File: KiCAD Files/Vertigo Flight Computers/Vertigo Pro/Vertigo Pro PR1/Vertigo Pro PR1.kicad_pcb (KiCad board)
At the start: 4 copper layers, 45.2 x 81.8 mm, 150 parts, among them IC1 ICM-20602, IC2 DPS310XTSA1, J1 ST-LINK Conn, J2 USB_C_2.0, J3 FFC2A32-24-T, J4 Screw_Terminal, J5 Screw_Terminal, J6 Screw_Terminal, J7 Screw_Terminal, Q1 MMBT3904-TP, Q2 MMBT3904-TP, Q3 FDN339AN, Q4 FDN339AN, Q5 SI7149ADP-T1-GE3, Q6 MMBT3904-TP, Q7 MMBT3904-TP, Q8 FDN339AN, Q9 FDN339AN, SW1 SW_SPDT, U1 STM32F103C8Tx, U10 TPS79133DBVR, U12 TLV709, U13 TLV75528PDBV, U2 AP63203WU, U3 ESP32-S3-WROOM-1, U4 TLV75515PDBV, U5 TLV709, U8 NEO-6M-GPS, U9 24AA32A-I_MS, Y1 16MHz

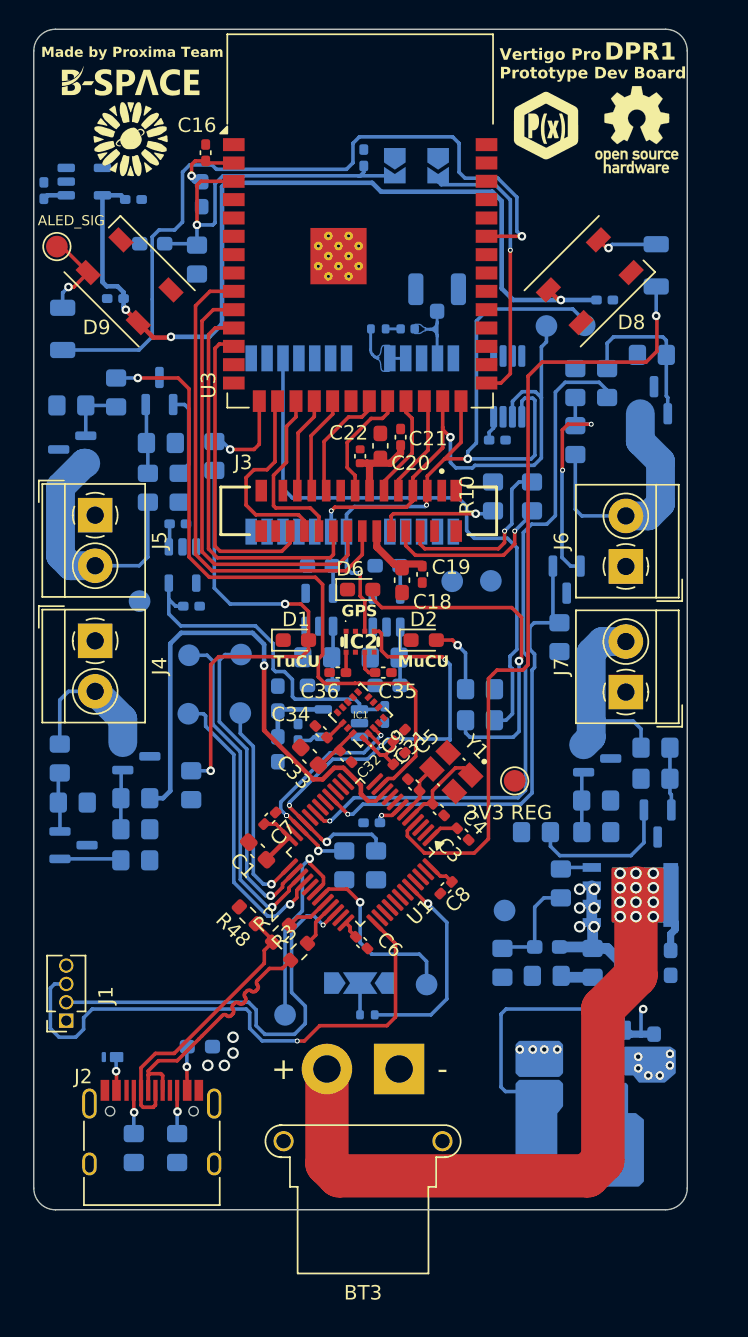
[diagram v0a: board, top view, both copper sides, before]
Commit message: Power routing
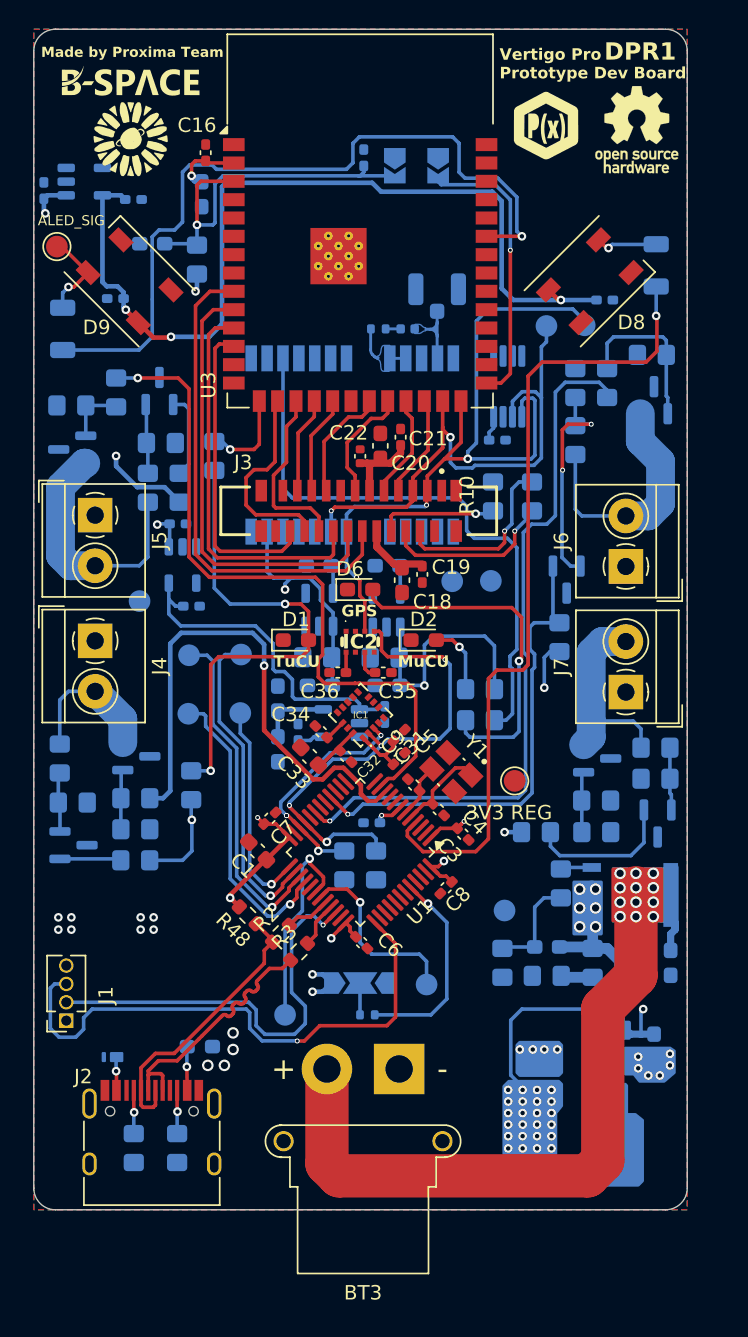
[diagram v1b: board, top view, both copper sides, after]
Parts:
- moved C24 0.07 mm to (145.7, 105.9)
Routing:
- net +3.3V: track 45.5 -> 99.4 mm, vias 1 -> 47
- net VCC: track 164.5 -> 194.5 mm, vias 11 -> 13
- net /ESP_I2C_SCL: track 72.3 -> 71.7 mm
- added copper zone on In2.Cu, net +3.3V
- added copper zone on B.Cu, net AGND
- added copper zone on F.Cu, net AGND
- added copper zone on In1.Cu, net AGND

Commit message: Much routing
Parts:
- moved ULN 7.78 mm to (141.1, 108.7)
- moved C33 0.28 mm to (144.9, 118.9)
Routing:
- net /CONTI_C2: track 5.93 -> 54.0 mm, vias 0 -> 3
- net /USB_VBUS_D_CUTOFF: track 12.1 -> 46.1 mm
- net /BATT_U: track 2.22 -> 34.2 mm, vias 0 -> 2
- net /IGN_4: track 0.00 -> 29.1 mm, vias 0 -> 3
- net /CONTI_C1: track 4.25 -> 25.7 mm, vias 0 -> 1
- net /ULN_3V3: track 9.88 -> 30.4 mm, vias 0 -> 5
- net /CONTI_C4: track 10.4 -> 28.5 mm, vias 0 -> 1
- net AGND: track 0.00 -> 5.29 mm, vias 10 -> 21
- net +3.3V: track 99.4 -> 102.3 mm, vias 47 -> 50
- net /SWCLK: track 38.8 -> 37.6 mm
- net /SWDIO: track 29.3 -> 30.4 mm
- net Net-(D1-A): track 33.9 -> 33.3 mm

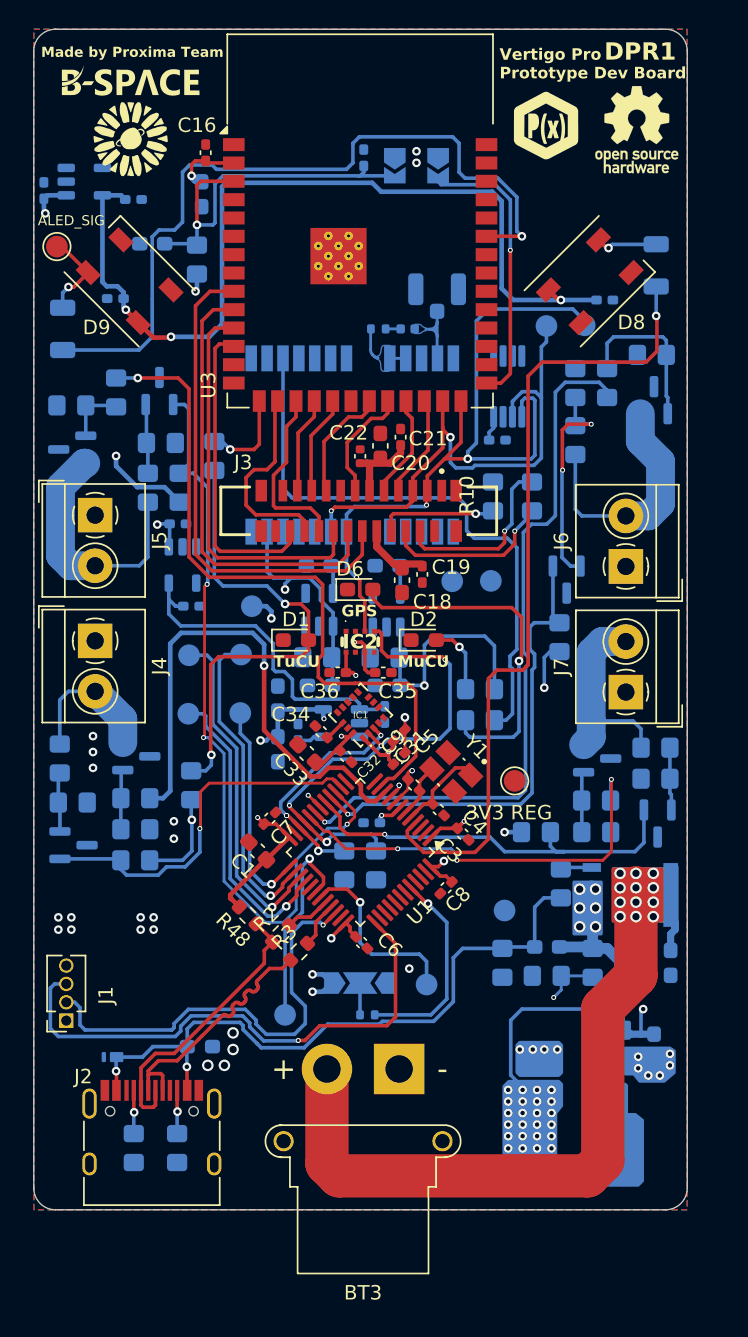
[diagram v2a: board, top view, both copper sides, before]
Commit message: Routing, EEPROM power fix + other stuff
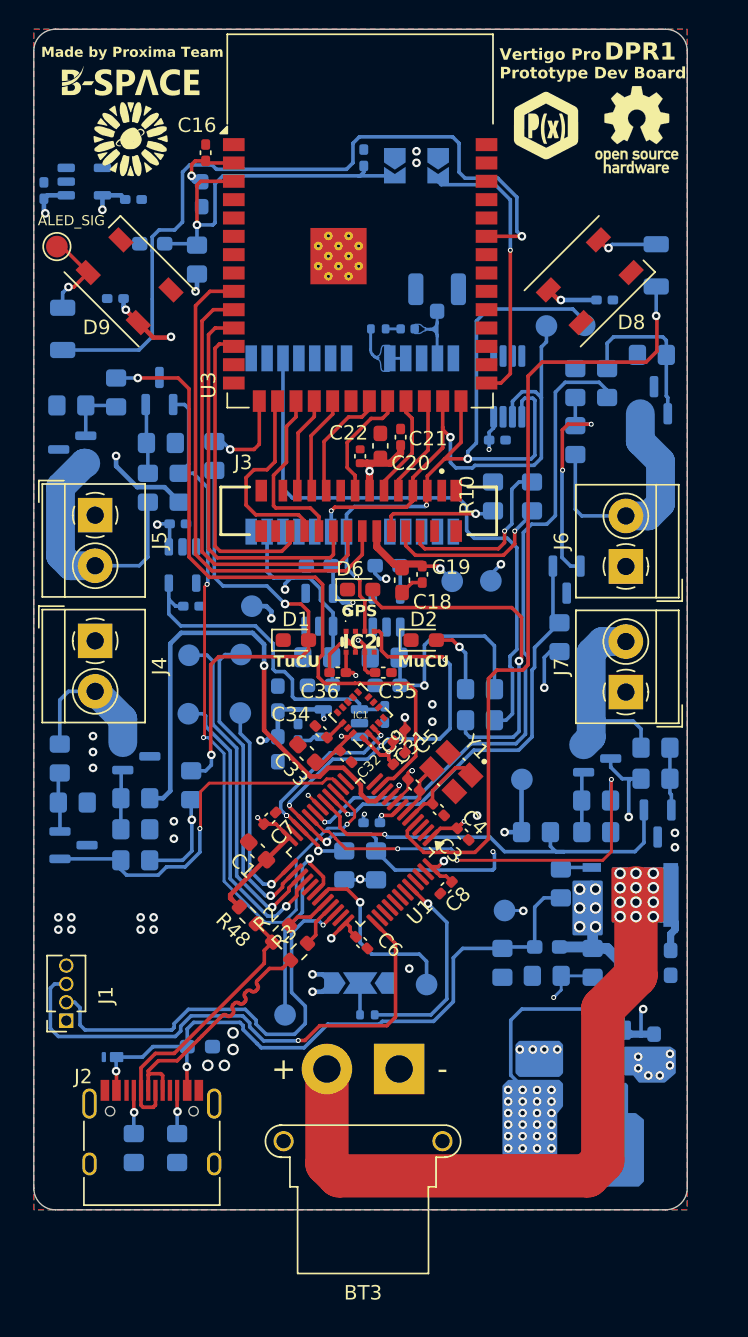
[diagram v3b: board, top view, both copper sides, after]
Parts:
- 3V3 REG: moved to B.Cu
- moved 3V3 REG 0.51 mm to (159.8, 120.7), turned to 180 degrees
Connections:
- C40 pad 2: Net-(U9-VCC) -> +3.3V
- U9 pad 8: Net-(U9-VCC) -> +3.3V
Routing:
- net /AVDD_2V8: track 20.2 -> 37.2 mm, vias 1 -> 3
- net AGND: track 5.29 -> 19.6 mm, vias 21 -> 30
- net /DVDD_1V5: track 6.74 -> 19.5 mm, vias 0 -> 2
- net /ESP_I2C_SCL: track 71.7 -> 81.8 mm, vias 6 -> 7
- net VCC: track 194.5 -> 202.9 mm, vias 13 -> 14
- net +3.3V: track 102.3 -> 110.4 mm, vias 50 -> 52
- net /ALED_PWR: track 62.1 -> 56.3 mm, vias 3 -> 4
- net /CONTI_C3: track 33.0 -> 29.4 mm
- net /IGN_3: track 49.7 -> 47.4 mm
- net Net-(U9-VCC): track 1.74 -> 0.00 mm

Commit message: Routing
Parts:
- added G***: LOGO, Vertigo Pro KiCad Libraries:proxima_logo_simple_footprint, B.Cu at (148.7, 72.2)
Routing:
- net AGND: track 19.6 -> 48.7 mm, vias 30 -> 49
- net /ESP_I2C_SDA: track 69.2 -> 82.4 mm, vias 7 -> 8
- net /ESP_I2C_SCL: track 81.8 -> 94.2 mm, vias 7 -> 8
- net /ULN_3V3: track 30.4 -> 31.4 mm
- net /AVDD_2V8: track 37.2 -> 37.9 mm
- net /CAM_RESET: track 11.9 -> 12.6 mm
- net VCC: track 202.9 -> 203.6 mm, vias 14 -> 16
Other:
- board text added: "Designed by Proxima Team"
- board text removed: "Made by Proxima Team"

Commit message: Routing
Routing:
- net /ESP_UART_TX: track 12.9 -> 77.9 mm, vias 1 -> 2
- net /ESP_UART_RX: track 14.7 -> 78.4 mm, vias 1 -> 2
- net AGND: track 48.7 -> 61.5 mm, vias 49 -> 56
- net /AVDD_2V8: track 37.9 -> 46.7 mm
- net Net-(U4-EN): track 0.00 -> 2.23 mm
- net Net-(U13-EN): track 0.00 -> 2.18 mm

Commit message: Routing
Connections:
- Q5 pad : (no net) -> Net-(BT3-+)
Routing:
- net AGND: track 61.5 -> 76.9 mm, vias 56 -> 69
- net +3.3V: track 110.4 -> 115.6 mm, vias 52 -> 54
- net /ESP_UART_TX: track 77.9 -> 78.9 mm

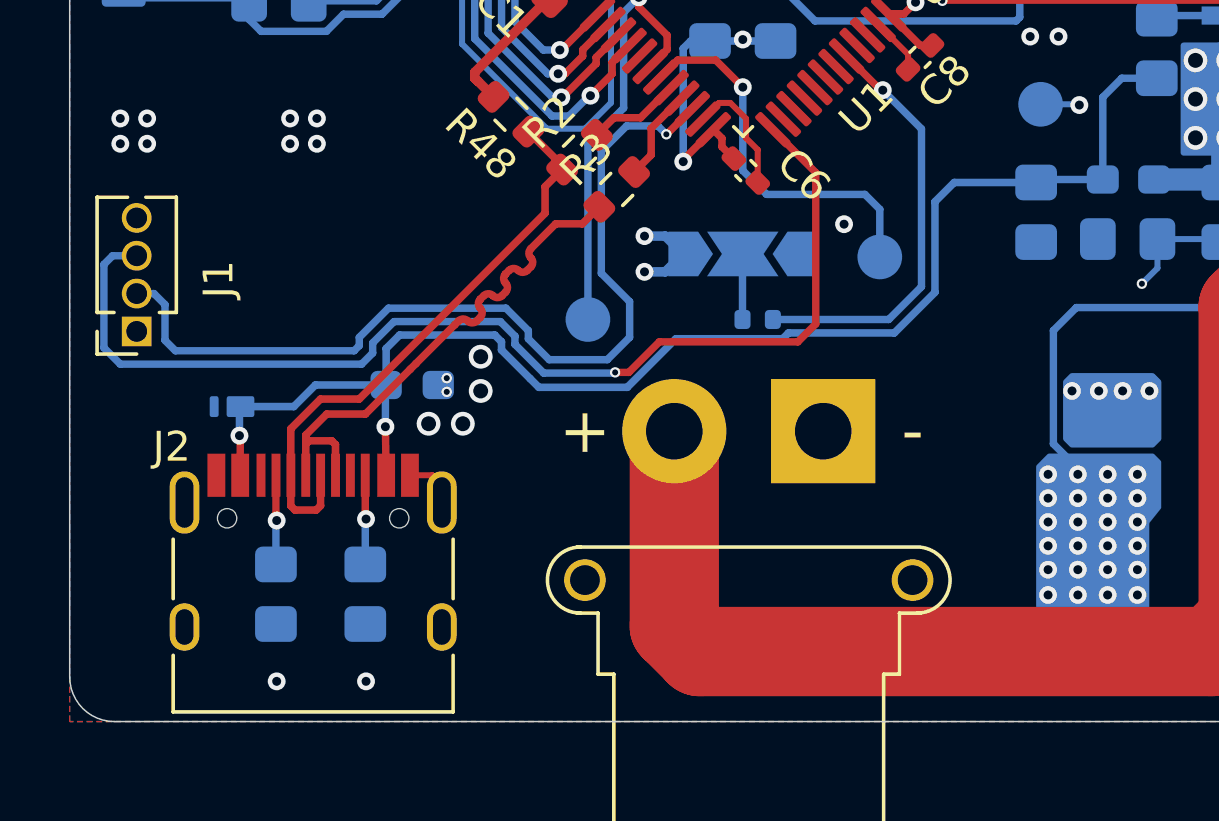
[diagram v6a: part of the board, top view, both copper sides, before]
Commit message: USB Diode fix
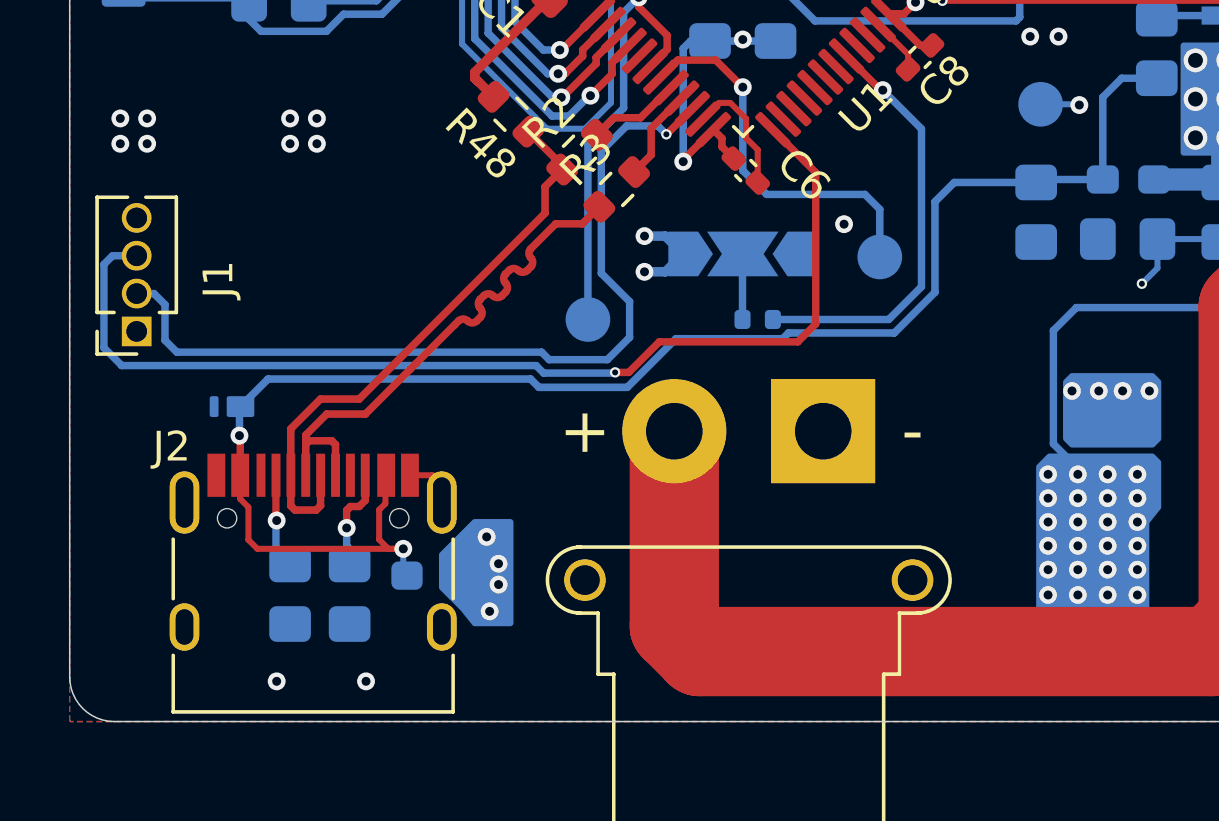
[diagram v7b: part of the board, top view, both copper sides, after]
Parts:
- moved D3 6.44 mm to (138.2, 145.6)
- moved R4 0.52 mm to (135.4, 146.2)
- moved R5 0.48 mm to (133.4, 146.2)
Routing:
- net /USB_VBUS_D_CUTOFF: track 46.1 -> 53.0 mm
- net VCC: track 203.6 -> 197.0 mm, vias 16 -> 14
- net /ALED_PWR: track 56.3 -> 61.2 mm
- net /SWCLK: track 37.6 -> 36.1 mm
- net /SWDIO: track 30.5 -> 29.0 mm
- net Net-(J2-CC2): track 3.09 -> 3.69 mm

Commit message: poprawki by marcin
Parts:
- J1: moved to B.Cu
- moved J1 7.08 mm to (131.5, 131.1)
- moved AE1 2.85 mm to (153.8, 84.4)
- moved R44 1.90 mm to (151.8, 89.5)
- moved L2 1.86 mm to (153.3, 88.3)
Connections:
- AE1 pad 2: (no net) -> AGND
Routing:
- net /SWCLK: track 36.1 -> 29.6 mm
- net +3.3V: track 115.6 -> 109.5 mm
- net /DVDD_1V5: track 19.5 -> 24.2 mm
- net Net-(AE1-A): track 4.54 -> 8.89 mm
- net /SWDIO: track 29.0 -> 26.6 mm
- net VCC: track 197.0 -> 198.5 mm
- net /AVDD_2V8: track 46.7 -> 45.9 mm
- net AGND: track 76.9 -> 76.7 mm, vias 69 -> 97
